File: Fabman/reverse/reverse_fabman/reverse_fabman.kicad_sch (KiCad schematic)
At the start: 184 parts, among them IC10 ISL8483EIBZ, J1 Conn_02x20_Counter_Clockwise, J2 Conn_01x40_MountingPin, J3 302-S101, J8 RJ45, SW1 SW_DPST_x2, SW2 SW_DPST_x2, SW3 SW_DPST_x2, T1 BUK9832-55A, T1 DMG2302U, T10 DMG2302U, T2 DMG2302U, T4 DMG2302U, T5 DMG2302U, T6 DMG2302U, T7 DMG2302U, T9 BUK9832-55A, U1 MCP23017_SS, U2 ESP32-WROOM-32D, U4 MCP23017_SS, Y1 XLH736022_579200I

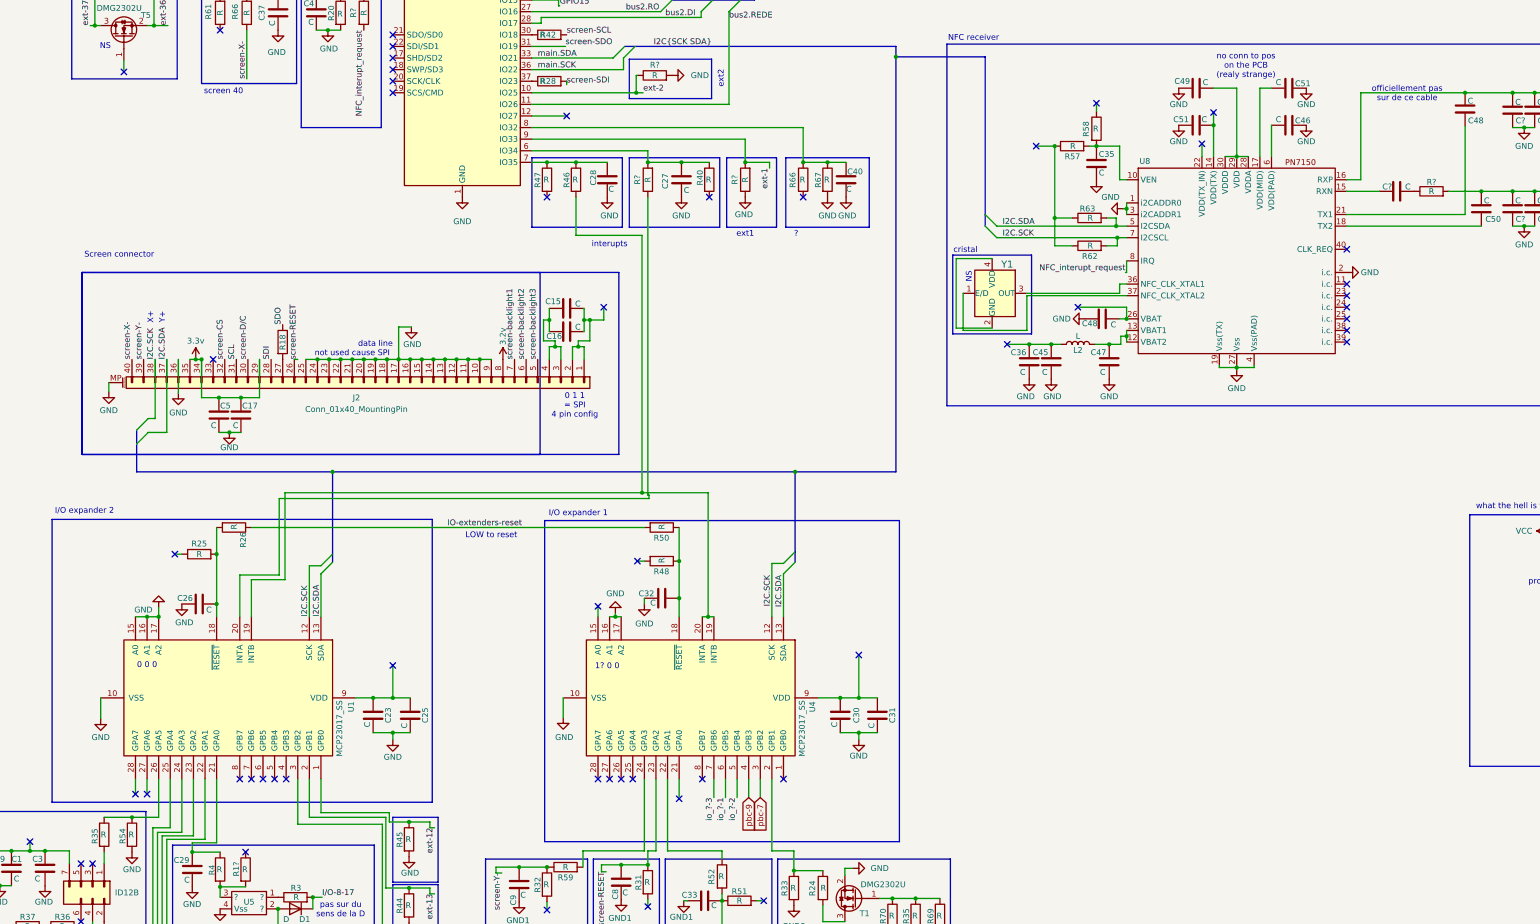
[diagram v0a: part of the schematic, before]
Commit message: - added original code serial output (i should dump the original binarry   maybe) - added demo (1 scan card screen (see figma), button/card event handler,   machine manual page) - updated schema - updated devkit case - added figma link
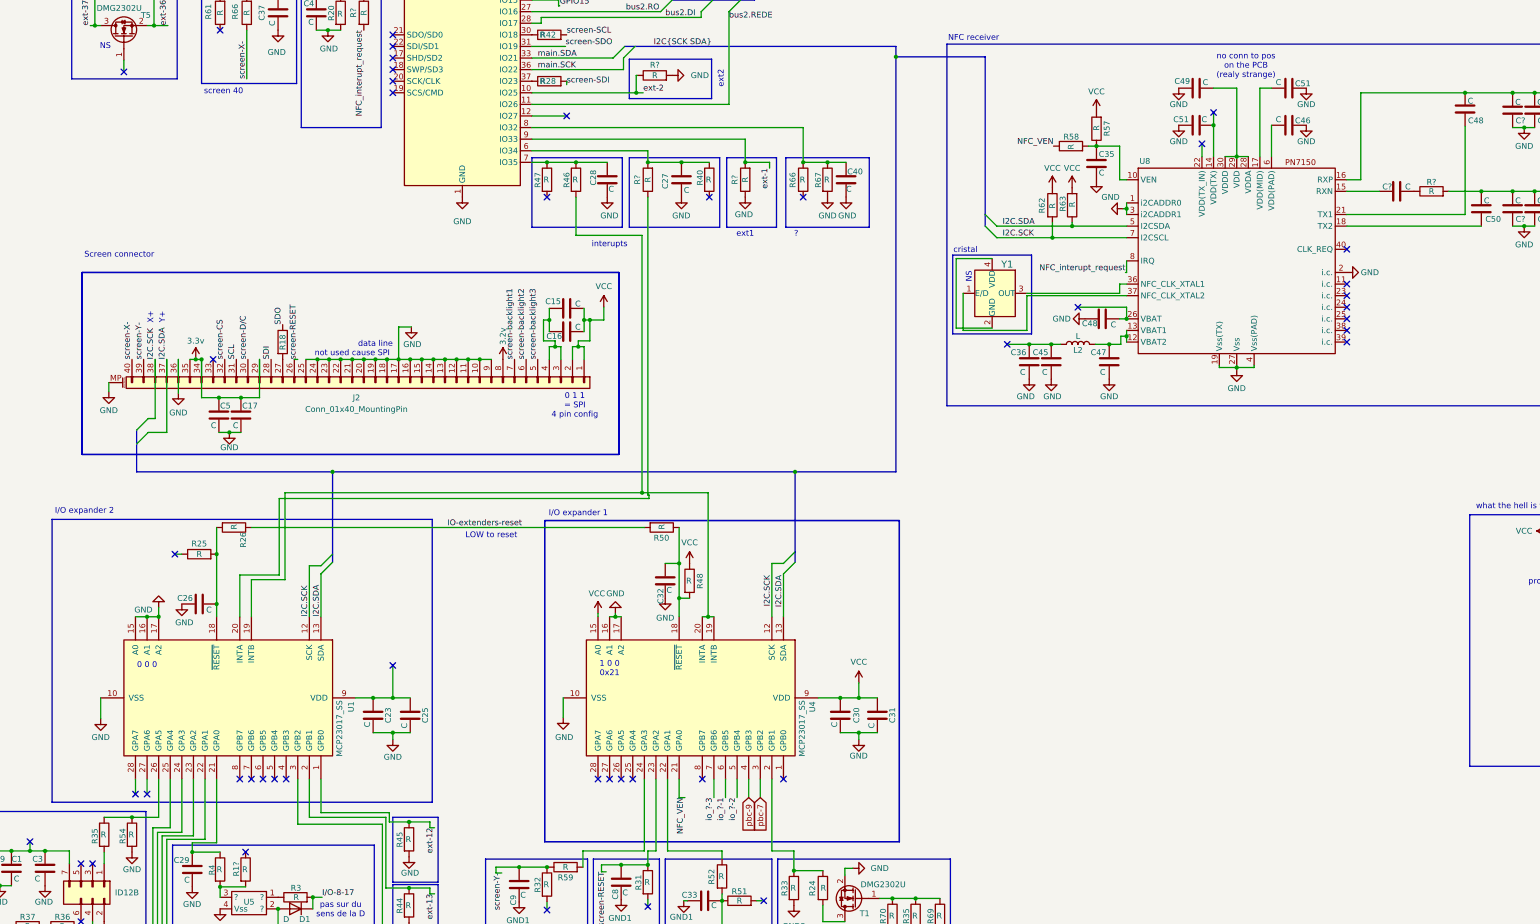
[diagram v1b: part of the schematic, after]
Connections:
- net I2C.SDA: now also R63.1; no longer R63.2
- net VCC: now also C15.2, C16.2, C30.1, C31.1, J2.1 (Pin_1), J2.2 (Pin_2), R48.1, R57.2, R62.1, R63.2, U4.15 (A0), U4.9 (VDD)
- net at C32.1, R50.1, U4.18 (~{RESET}): now also R48.2; no longer R48.1
- net NFC_VEN: now reaches U4.21 (GPA0)
- net NFC_VEN: now also R58.1
- net at C35.1, R58.2, U8.10 (VEN): now also R57.1; no longer R57.2
- no-connect marks 84 -> 77
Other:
- note added: "1 0 0 0x21"
- note removed: "1? 0 0"
- note removed: "officiellement pas sur de ce cable"
- moved on the sheet: C32, R48, R57, R58, R62, R63
